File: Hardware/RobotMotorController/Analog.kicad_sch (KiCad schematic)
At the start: 32 parts, among them U3 #DS18B20, U4 #DS18B20, U5 #DS18B20, U6 #DS18B20

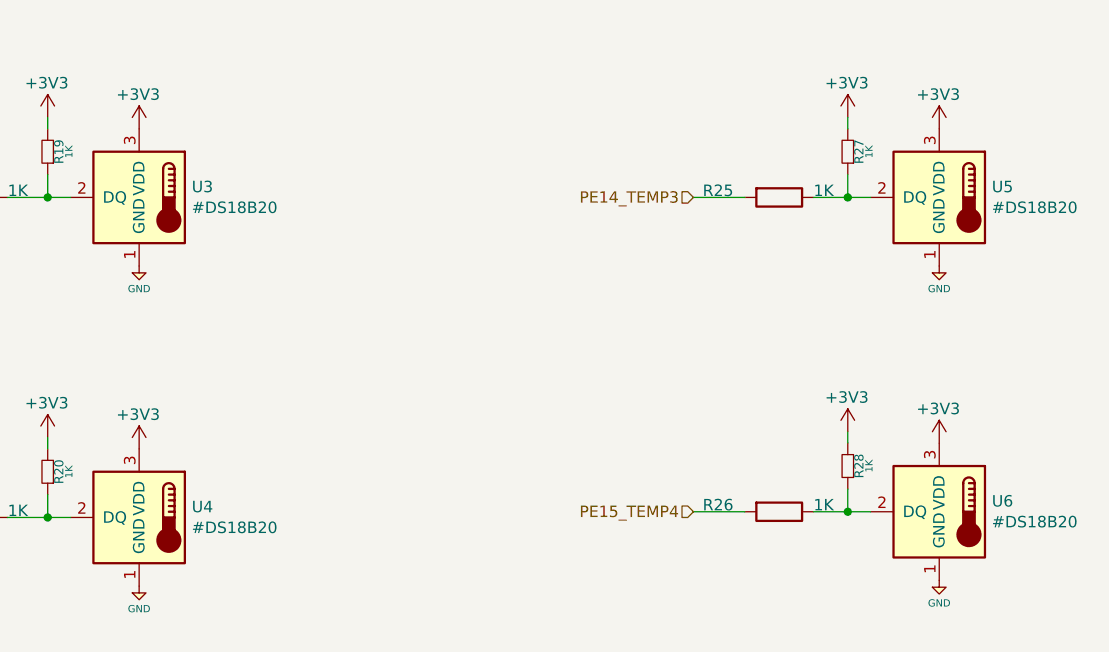
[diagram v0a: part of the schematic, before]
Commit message: General update, first encoder implementation
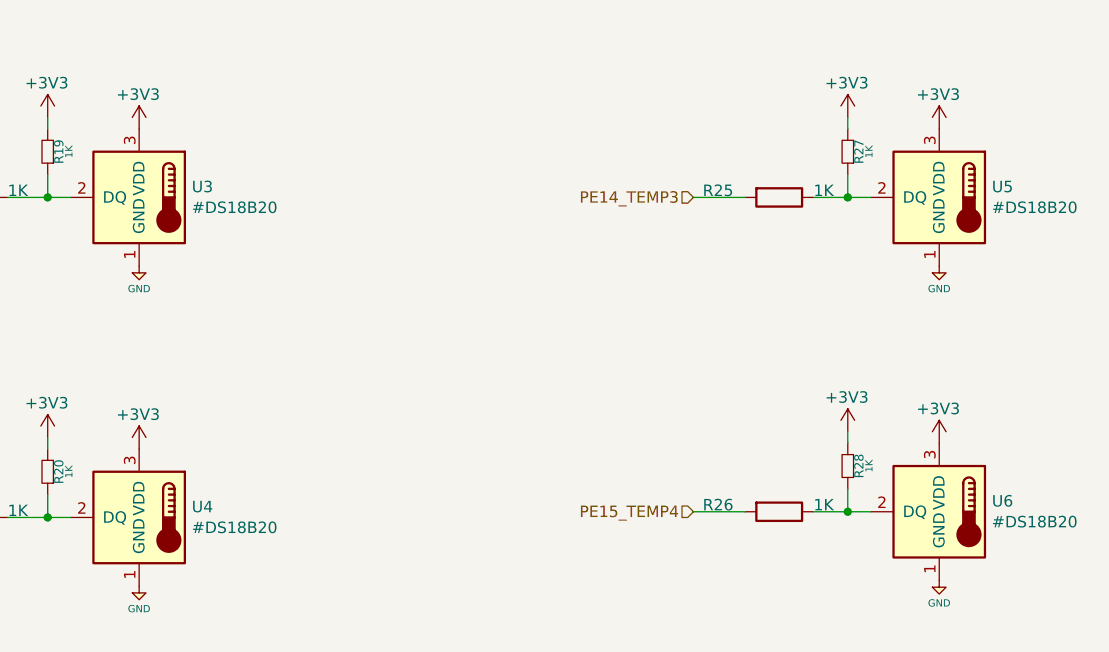
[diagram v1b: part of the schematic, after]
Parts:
- R19, R20, R27, R28: Spice_Model 1k -> (none); Spice_Netlist_Enabled Y -> (none); Spice_Primitive R -> (none)
